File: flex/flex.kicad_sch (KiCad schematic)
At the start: 27 parts, among them J1 Conn_01x06_Female, J2 Conn_01x03_Female, J3 Conn_01x01_Female, SW1 SW_Push, SW14 SW_Push, SW19 SW_Push, SW5 SW_Push, SW9 SW_Push

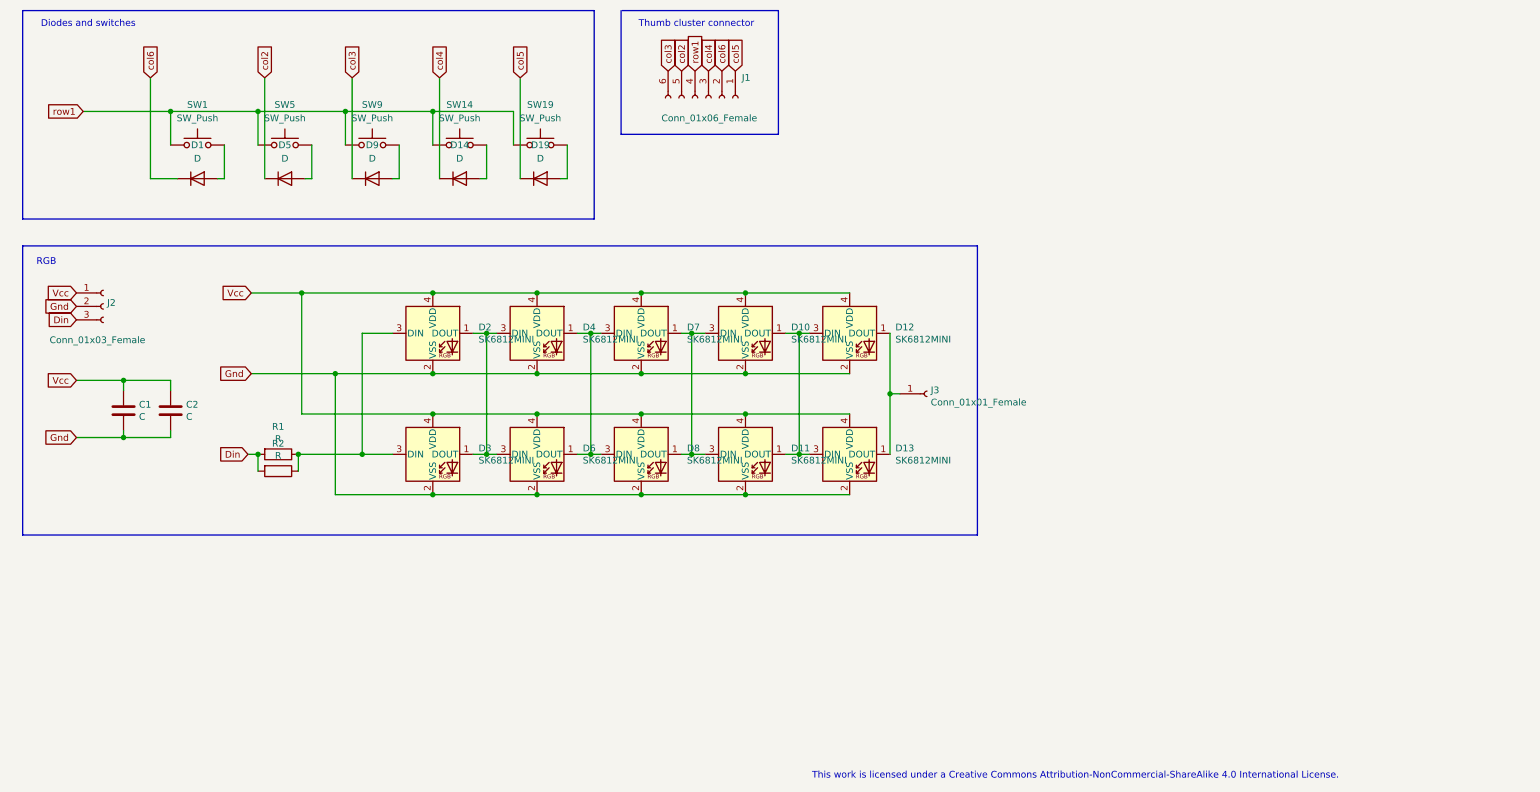
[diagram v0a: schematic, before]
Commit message: vcc gnd routing
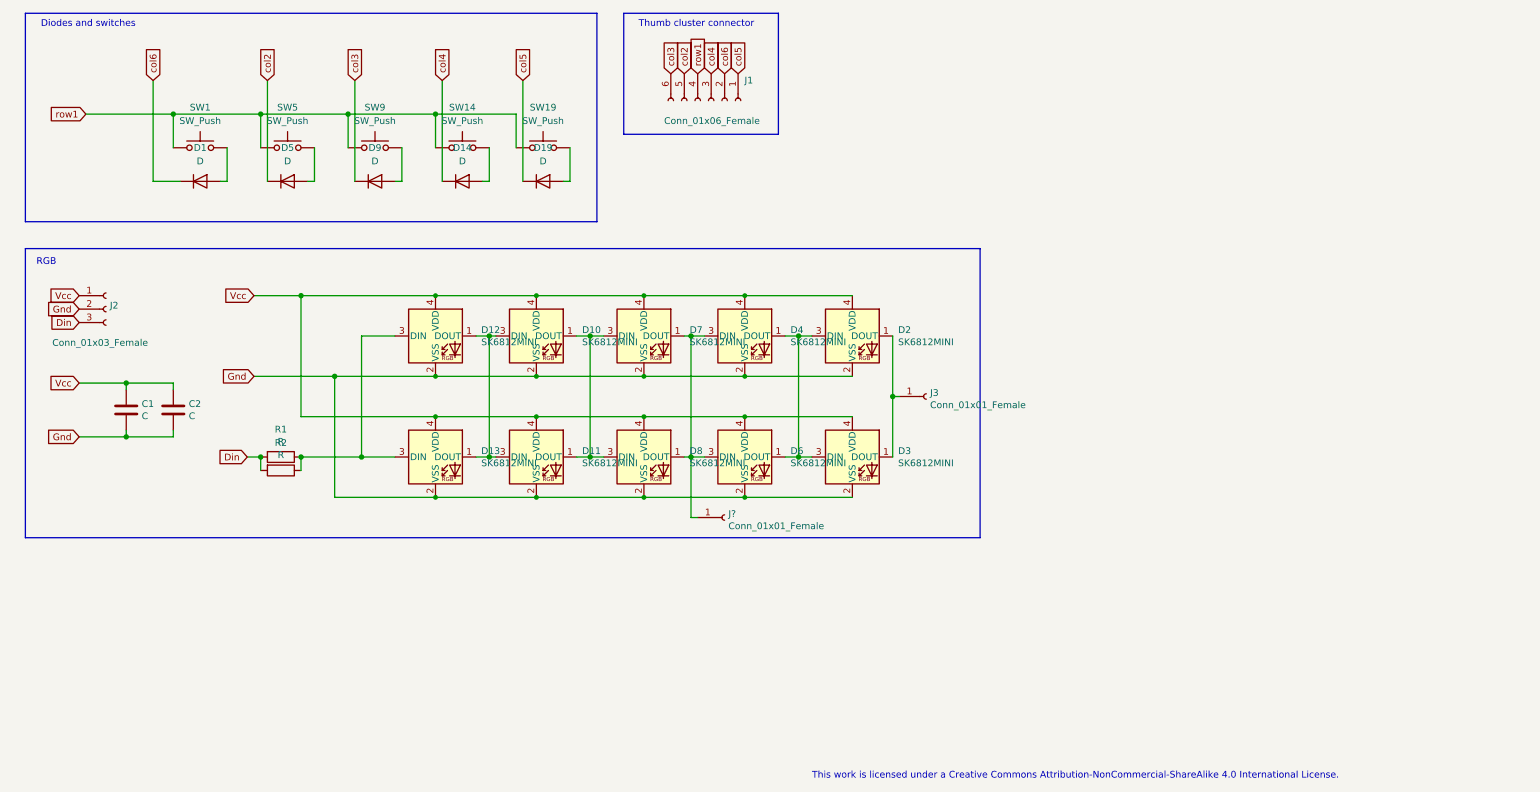
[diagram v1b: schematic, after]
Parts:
- added J?: Conn_01x01_Female, Connector_PinHeader_2.54mm:PinHeader_1x01_P2.54mm_Vertical, symbol Connector:Conn_01x01_Female
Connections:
- net at D12.1 (DOUT), D13.1 (DOUT): now also D10.3 (DIN), D11.3 (DIN); no longer J3.1 (Pin_1)
- net at D12.3 (DIN), D13.3 (DIN): now also R1.1, R2.1; no longer D10.1 (DOUT), D11.1 (DOUT)
- net at D7.1 (DOUT), D8.1 (DOUT): now also D4.3 (DIN), D6.3 (DIN), J?.1 (Pin_1); no longer D10.3 (DIN), D11.3 (DIN)
- net at D2.3 (DIN), D3.3 (DIN): now also D4.1 (DOUT), D6.1 (DOUT); no longer R1.1, R2.1
- net at D7.3 (DIN), D8.3 (DIN): now also D10.1 (DOUT), D11.1 (DOUT); no longer D4.1 (DOUT), D6.1 (DOUT)
- net at D2.1 (DOUT), D3.1 (DOUT): now also J3.1 (Pin_1); no longer D4.3 (DIN), D6.3 (DIN)
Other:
- moved on the sheet: C1, C2, D1, D10, D11, D12, D13, D14, D19, D2, D3, D4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
